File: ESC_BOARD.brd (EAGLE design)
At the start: 139.7 x 40.6 mm, 37 parts, among them J5 284512-3-180, J6 284512-3-180, J7 284512-3-180, J8 284512-3-180, U1 SN74CBTLV3257PWR, Y1 ECS-80-S-4X

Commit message: resistor ID added and changed SWD connections
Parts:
- removed C12: 0.1uF, SparkFun-Capacitors:0603
- removed U1: SN74CBTLV3257PWR, SN74CBTLV3257PWR:SN74CBTLV3257PWR
- R4: value 1.5k -> 1k
- moved R4 83.5 mm to (-3.30, -26.4), flipped to the top, turned to 0 degrees
- moved SV2 11.9 mm to (67.1, 46.7)
- moved J7 3.42 mm to (135.9, 28.7)
- moved J8 2.34 mm to (3.05, 29.2)
- moved J5 2.05 mm to (135.9, 12.7)
- moved J6 2.05 mm to (2.79, 12.2)
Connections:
- removed net !RST_IN: U$1.P$20, U1.P$9
- removed net NRST1: C7.1, R2.1, RESET.2, U$4.NRST
- removed net PROG_SEL: R4.1, U$1.P$5, U1.P$15
- removed net SWCLK_IN: U$1.P$22, U1.P$4
- removed net SWDIO_IN: U$1.P$21, U1.P$7
- new net RES_ID: R4.1, U$1.P$19, U$4.PA0
- net !RST: now also C7.1, R2.1, RESET.2, U$1.P$20, U$4.NRST; no longer U1.P$11
- net +3V3: no longer C12.1, U1.P$16
- net GND: no longer C12.2, U1.P$1, U1.P$8
- net SWCLK: now also U$1.P$22; no longer U1.P$2
- net SWDIO: now also U$1.P$21; no longer U1.P$5

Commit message: placed most components
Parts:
- removed C3: 4.7uF, SparkFun-Capacitors:0603
- removed J1: (no value), SparkFun-Connectors:1X08
- moved JP4 168.5 mm to (81.3, 16.3), turned to 180 degrees
- moved JP3 164.0 mm to (81.0, 29.2), turned to 180 degrees
- moved J8 134.8 mm to (136.7, 10.9), flipped to the bottom
- moved U$8 133.7 mm to (74.4, 22.9)
- moved J5 133.3 mm to (3.81, 30.5), flipped to the bottom
- moved C10 131.3 mm to (72.6, 24.6), turned to 90 degrees
- moved C7 129.8 mm to (77.5, 35.6)
- moved R2 129.7 mm to (72.4, 35.3), turned to 180 degrees
- moved JP2 129.3 mm to (57.7, 15.5)
- moved C9 127.6 mm to (71.6, 6.35), flipped to the bottom, turned to 180 degrees
- moved JP1 127.4 mm to (57.4, 31.0)
- moved U$4 125.5 mm to (70.9, 12.7), turned to 90 degrees
- moved C4 121.5 mm to (67.3, 14.0), flipped to the bottom, turned to 90 degrees
- moved C5 120.0 mm to (69.1, 14.0), flipped to the bottom, turned to 90 degrees
- moved R1 119.4 mm to (68.6, 10.2), turned to 180 degrees
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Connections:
- removed net CURRENT_ADC: J1.6
- removed net TLM/RX2: J1.5
- net +12V: no longer J1.8
- net +3V3: no longer C3.1
- net ESC_PWM_1: no longer J1.4
- net ESC_PWM_2: no longer J1.3
- net ESC_PWM_3: no longer J1.2
- net ESC_PWM_4: no longer J1.1
- net GND: no longer C3.2, J1.7
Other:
- board size 139.7 x 40.6 mm -> 140.2 x 39.6 mm

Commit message: routed for rev2
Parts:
- removed D1: (no value), SparkFun-LED:LED-0603
- removed RESET: (no value), DiscreteComponents:SW_2512
- added U$2: MURATA-DC-DC, MURATA_3pin_dcdc:MURATA-DC-DC
- added U$3: DISCRETECOMPONENTS_SWITCH, Push button - FSM2JMTR:DISCRETECOMPONENTS_SW_2512
- added U$5: LED-0805, LED-0805:0805
- moved R2 6.38 mm to (66.0, 34.7), turned to 90 degrees
- moved JP1 4.49 mm to (59.6, 27.1)
- moved C7 3.64 mm to (78.2, 32.0)
- moved J8 2.16 mm to (136.5, 8.76)
- moved J5 1.89 mm to (2.41, 31.8), turned to 270 degrees
- moved R4 1.70 mm to (79.8, 21.1)
- moved J6 1.55 mm to (2.54, 11.3), turned to 270 degrees
- moved C9 1.30 mm to (71.9, 7.62), flipped to the top, turned to 0 degrees
- moved SV2 1.30 mm to (68.8, 31.5)
- moved JP3 1.27 mm to (79.8, 29.2)
- moved C8 1.17 mm to (61.2, 7.49), flipped to the top, turned to 180 degrees
- moved Y1 1.14 mm to (66.5, 7.49), flipped to the bottom, turned to 180 degrees
- moved JP4 0.72 mm to (80.8, 16.8)
- moved JP2 0.57 mm to (58.2, 15.2)
- moved R3 0.25 mm to (64.5, 10.2)
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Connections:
- net !RST: now also U$3.2; no longer RESET.2
- net +12V: now also U$2.1
- net +3V3: now also U$2.3
- net ESC1_B: now also J5.1; no longer J5.3
- net ESC1_R: now also J5.3; no longer J5.1
- net ESC2_B: now also J6.1; no longer J6.3
- net ESC2_R: now also J6.3; no longer J6.1
- net GND: now also U$2.2, U$3.1, U$5.C; no longer D1.C, RESET.1
- net N$24: now also U$5.A; no longer D1.A
- net TIM3_CH1: now also U$4.PA7; no longer U$4.PA6
- net TIM3_CH2: now also U$4.PA6; no longer U$4.PA7
- net TIM3_CH3: now also U$4.PB1; no longer U$4.PB0
- net TIM3_CH4: now also U$4.PB0; no longer U$4.PB1
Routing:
- net +3V3: track 0.00 -> 83.1 mm, vias 0 -> 4
- net +12V: track 0.00 -> 71.8 mm, vias 0 -> 28
- net !RST: track 0.00 -> 56.8 mm
- net SWDIO: track 0.00 -> 36.7 mm, vias 0 -> 3
- net SWCLK: track 0.00 -> 36.2 mm, vias 0 -> 2
- net RES_ID: track 0.00 -> 25.8 mm, vias 0 -> 1
- net ESC_PWM_1: track 0.00 -> 20.7 mm, vias 0 -> 1
- net TIM3_CH1: track 0.00 -> 18.8 mm, vias 0 -> 2
- net GND: track 0.00 -> 16.3 mm, vias 0 -> 36
- net ESC_PWM_4: track 0.00 -> 16.1 mm, vias 0 -> 1
- net TIM3_CH2: track 0.00 -> 15.4 mm, vias 0 -> 2
- net TIM3_CH3: track 0.00 -> 15.0 mm, vias 0 -> 1
- net ESC_PWM_2: track 0.00 -> 12.7 mm, vias 0 -> 1
- net ESC_PWM_3: track 0.00 -> 11.9 mm, vias 0 -> 1
- net CAN_TX: track 0.00 -> 11.4 mm
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- added copper zone on layer 1, net +12V
- added copper zone on layer 16, net +12V
- added copper zone on layer 1, net +3V3
- added copper zone on layer 16, net +3V3
- added copper zone on layer 1, net ESC1_B
- added copper zone on layer 16, net ESC1_B
- added copper zone on layer 1, net ESC1_R
- added copper zone on layer 16, net ESC1_R
- added copper zone on layer 1, net ESC1_Y
- added copper zone on layer 16, net ESC1_Y
- added copper zone on layer 1, net ESC2_B
- added copper zone on layer 16, net ESC2_B
- added copper zone on layer 1, net ESC2_R
- added copper zone on layer 16, net ESC2_R
- added copper zone on layer 1, net ESC2_Y
- added copper zone on layer 16, net ESC2_Y
- added copper zone on layer 1, net ESC3_B
- added copper zone on layer 16, net ESC3_B
- added copper zone on layer 1, net ESC3_R
- added copper zone on layer 16, net ESC3_R
- added copper zone on layer 1, net ESC3_Y
- added copper zone on layer 16, net ESC3_Y
- added copper zone on layer 1, net ESC4_B
- added copper zone on layer 16, net ESC4_B
- added copper zone on layer 1, net ESC4_R
- added copper zone on layer 16, net ESC4_R
- added copper zone on layer 1, net ESC4_Y
- added copper zone on layer 16, net ESC4_Y
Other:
- board size 140.2 x 39.6 mm -> 139.2 x 39.9 mm
- board text added: "ROV X12.5 Quad ESC v2 Grant Geyer 10/23/20"
- board text removed: "ROV X12.5 Quad ESC v2 Grant Geyer"

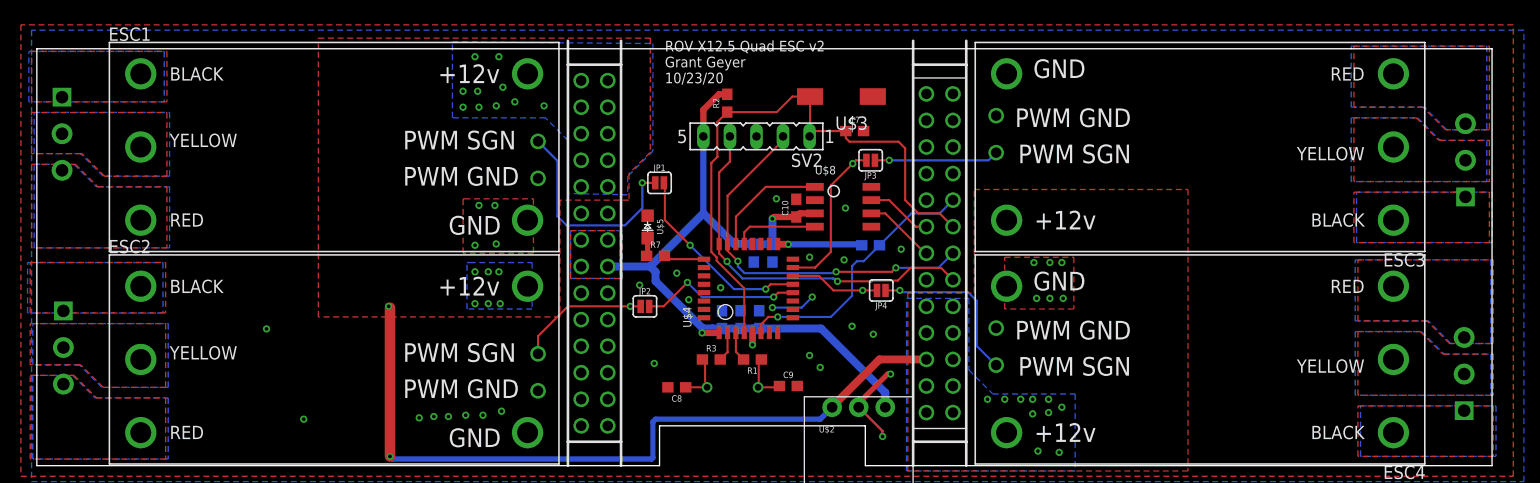
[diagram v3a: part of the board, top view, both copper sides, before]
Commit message: connector CAD and a few touchups
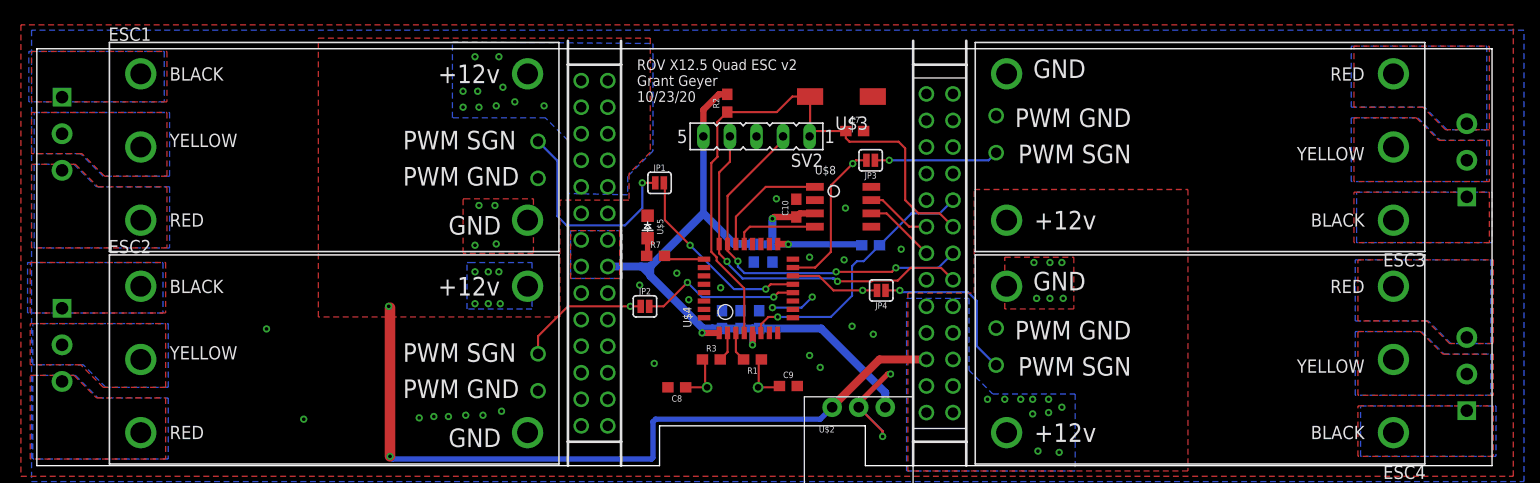
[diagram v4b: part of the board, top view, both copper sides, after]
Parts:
- removed J5, J6, J7, J8: 284512-3-180, TE 3 pin 3.5mm:TE_284512-3-180
- removed U$1: ESC2BACKPLANE, ESC_to_Backplane_Connectors:ESC2BACKPLANE_WHOLE
- added J1, J2, J3, J4: TE_2351886-3-(VERT), TE 3 pin 3.5mm:TE_2351886-3-(VERT)
- added U$6: ESC2BACKPLANE, ESC_to_Backplane_Connectors_esc:ESC2BACKPLANE_WHOLE
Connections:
- net !RST: now also U$6.P$20; no longer U$1.P$20
- net +12V: now also U$6.P$10, U$6.P$11, U$6.P$12, U$6.P$13, U$6.P$23, U$6.P$24, U$6.P$25, U$6.P$26, U$6.P$27, U$6.P$9, U$6.P$A, U$6.P$B, U$6.P$C, U$6.P$D, U$6.P$E, U$6.P$O, U$6.P$P, U$6.P$Q, U$6.P$R, U$6.P$S; no longer U$1.P$10, U$1.P$11, U$1.P$12, U$1.P$13, U$1.P$23, U$1.P$24, U$1.P$25, U$1.P$26, U$1.P$27, U$1.P$9, U$1.P$A, U$1.P$B, U$1.P$C, U$1.P$D, U$1.P$E, U$1.P$O, U$1.P$P, U$1.P$Q, U$1.P$R, U$1.P$S
- net +3V3: now also U$6.P$G, U$6.P$H, U$6.P$U, U$6.P$V; no longer U$1.P$G, U$1.P$H, U$1.P$U, U$1.P$V
- net CAN_H: now also U$6.P$6; no longer U$1.P$6
- net CAN_L: now also U$6.P$7; no longer U$1.P$7
- net ESC1_B: now also J1.1; no longer J5.1
- net ESC1_R: now also J1.3; no longer J5.3
- net ESC1_Y: now also J1.2; no longer J5.2
- net ESC2_B: now also J4.1; no longer J6.1
- net ESC2_R: now also J4.3; no longer J6.3
- net ESC2_Y: now also J4.2; no longer J6.2
- net ESC3_B: now also J2.1; no longer J7.1
- net ESC3_R: now also J2.3; no longer J7.3
- net ESC3_Y: now also J2.2; no longer J7.2
- net ESC4_B: now also J3.1; no longer J8.1
- net ESC4_R: now also J3.3; no longer J8.3
- net ESC4_Y: now also J3.2; no longer J8.2
- net GND: now also U$6.P$1, U$6.P$15, U$6.P$16, U$6.P$17, U$6.P$18, U$6.P$2, U$6.P$3, U$6.P$4, U$6.P$AA, U$6.P$BB, U$6.P$J, U$6.P$K, U$6.P$L, U$6.P$M, U$6.P$N, U$6.P$X, U$6.P$Y, U$6.P$Z; no longer U$1.P$1, U$1.P$15, U$1.P$16, U$1.P$17, U$1.P$18, U$1.P$2, U$1.P$3, U$1.P$4, U$1.P$AA, U$1.P$BB, U$1.P$J, U$1.P$K, U$1.P$L, U$1.P$M, U$1.P$N, U$1.P$X, U$1.P$Y, U$1.P$Z
- net RES_ID: now also U$6.P$19; no longer U$1.P$19
- net SWCLK: now also U$6.P$22; no longer U$1.P$22
- net SWDIO: now also U$6.P$21; no longer U$1.P$21
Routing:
- net +3V3: track 83.1 -> 84.4 mm
